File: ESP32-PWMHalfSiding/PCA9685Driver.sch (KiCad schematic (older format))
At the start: 18 parts, among them P601 C A0 A1 A2 A3 A4 A5 A6 A7, P602 C B0 B1 B2 B3 B4 B5 B6 B7, T601 + 12V -, U601 PCA9685, U602 TBD62X83A, U603 TBD62X83A

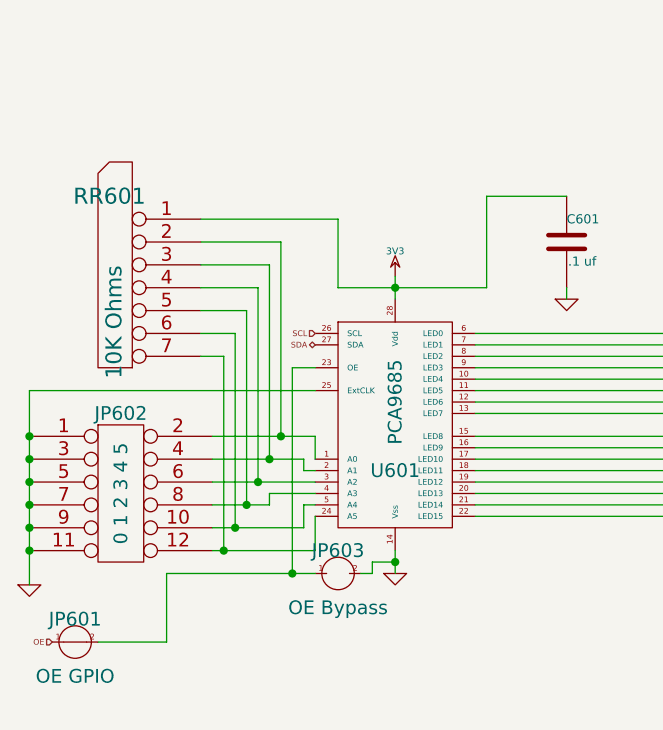
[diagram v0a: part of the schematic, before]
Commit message: Remove unneeded address jumpers from ESP32-PWMHalfSiding and fixup board part labels.
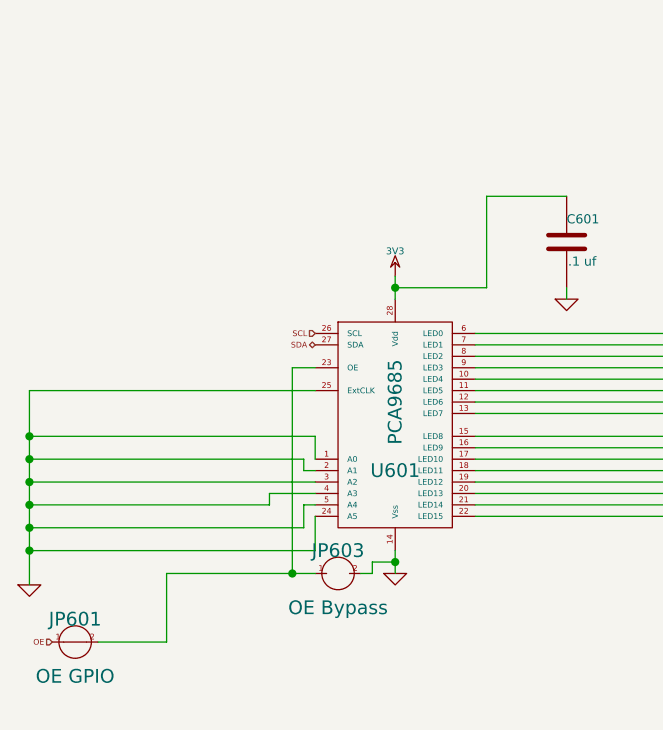
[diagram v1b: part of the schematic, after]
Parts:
- removed JP602: 0 1 2 3 4 5, ~, symbol CONN_6X2
- removed RR601: 10K Ohms, ~, symbol RR6
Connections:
- net GND: now also U601.1 (A0), U601.2 (A1), U601.24 (A5), U601.3 (A2), U601.4 (A3), U601.5 (A4)
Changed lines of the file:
@@
 Sheet 6 6
 Title ""
-Date "1 feb 2020"
+Date "9 feb 2020"
 Rev ""
 Comp ""
@@
 $EndComp
 $Comp
-L CONN_6X2 JP602
-U 1 1 5E35CA23
-P 1600 2700
-F 0 "JP602" H 1600 3050 60  0000 C CNN
-F 1 "0  1  2  3  4  5" V 1600 2700 60  0000 C CNN
-F 2 "~" H 1600 2700 60  0000 C CNN
-F 3 "~" H 1600 2700 60  0000 C CNN
-	1    1600 2700
-	1    0    0    -1
-$EndComp
-$Comp
 L GND #PWR033
 U 1 1 5E35CA24
@@
 $EndComp
 $Comp
-L RR6 RR601
-U 1 1 5E35CA25
-P 1600 1950
-F 0 "RR601" H 1650 2500 70  0000 C CNN
-F 1 "10K Ohms" V 1630 1950 70  0000 C CNN
-F 2 "~" H 1600 1950 60  0000 C CNN
-F 3 "~" H 1600 1950 60  0000 C CNN
-	1    1600 1950
-	-1   0    0    -1
-$EndComp
-$Comp
 L CLOSED JP601
 U 1 1 5E35CA26
@@
 	3200 1800 3200 1400
 Wire Wire Line
-	2550 1800 3200 1800
+	2800 1800 3200 1800
 Connection ~ 2800 1800
 Wire Wire Line
@@
 	5050 4900 5000 4900
 Wire Wire Line
-	1950 1500 2550 1500
-Wire Wire Line
-	2550 1500 2550 1800
-Wire Wire Line
-	2000 2450 2450 2450
+	1200 2450 2450 2450
 Wire Wire Line
 	2450 2450 2450 2550
 Wire Wire Line
-	2000 2950 2450 2950
+	1200 2950 2450 2950
 Wire Wire Line
 	2450 2950 2450 2800
@@
 	2450 2600 2400 2600
 Wire Wire Line
-	2400 2600 2400 2550
-Wire Wire Line
-	2400 2550 2000 2550
+	2400 2550 2400 2600
+Wire Wire Line
+	1200 2550 2400 2550
 Wire Wire Line
 	2450 2750 2400 2750
 Wire Wire Line
-	2400 2850 2000 2850
+	1200 2850 2400 2850
 Wire Wire Line
 	2250 2700 2450 2700
 Wire Wire Line
-	2000 2650 2450 2650
-Wire Wire Line
-	1950 2100 2050 2100
-Wire Wire Line
-	2050 2100 2050 2950
-Connection ~ 2050 2950
-Wire Wire Line
-	1950 2000 2100 2000
-Wire Wire Line
-	2100 2000 2100 2850
-Connection ~ 2100 2850
-Wire Wire Line
-	2150 2750 2150 1900
-Wire Wire Line
-	2150 1900 1950 1900
-Connection ~ 2150 2750
-Wire Wire Line
-	1950 1800 2200 1800
-Connection ~ 2200 2650
-Wire Wire Line
-	2250 2550 2250 1700
-Wire Wire Line
-	2250 1700 1950 1700
-Connection ~ 2250 2550
-Wire Wire Line
-	1950 1600 2300 1600
-Wire Wire Line
-	2300 1600 2300 2450
-Connection ~ 2300 2450
+	1200 2650 2450 2650
 Wire Wire Line
 	1200 2250 1200 3100
@@
 Connection ~ 2800 3000
 Wire Wire Line
-	2400 2750 2400 2850
-Wire Wire Line
-	2200 1800 2200 2650
-Wire Wire Line
-	2250 2700 2250 2750
-Wire Wire Line
-	2250 2750 2000 2750
+	2400 2850 2400 2750
+Wire Wire Line
+	2250 2750 2250 2700
+Wire Wire Line
+	1200 2750 2250 2750
 Connection ~ 2350 3050
 Wire Wire Line

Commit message: BOM for ESP32-PWMHalfSiding
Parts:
- C601: Mouser Part Number (none) -> 21RZ310-RC
- D601: Mouser Part Number (none) -> 625-SB240-E3
- P601, P602: Mouser Part Number (none) -> 651-1725724
- RP601, RP602: Mouser Part Number (none) -> 652-4116R-1LF-1.5K
- T601: Mouser Part Number (none) -> 651-1725656
- U601: Mouser Part Number (none) -> 771-PCA9685PW,118
- U602, U603: Mouser Part Number (none) -> 757-TBD62083APG or 757-TBD62783APG
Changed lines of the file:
@@
 Sheet 6 6
 Title ""
-Date "9 feb 2020"
+Date "11 feb 2020"
 Rev ""
 Comp ""
@@
 F 2 "~" H 2800 2400 60  0000 C CNN
 F 3 "~" H 2800 2400 60  0000 C CNN
+F 4 " 771-PCA9685PW,118" H 2800 2400 60  0001 C CNN "Mouser Part Number"
 	1    2800 2400
 	1    0    0    -1
@@
 F 2 "~" H 3588 1450 30  0000 C CNN
 F 3 "~" H 3550 1600 60  0000 C CNN
+F 4 "21RZ310-RC" H 3550 1600 60  0001 C CNN "Mouser Part Number"
 	1    3550 1600
 	1    0    0    -1
@@
 F 2 "~" H 4800 1100 60  0000 C CNN
 F 3 "~" H 4800 1100 60  0000 C CNN
+F 4 " 757-TBD62083APG or 757-TBD62783APG" H 4800 1100 60  0001 C CNN "Mouser Part Number"
 	1    4800 1100
 	1    0    0    -1
@@
 F 2 "~" H 7300 1050 60  0000 C CNN
 F 3 "~" H 7300 1050 60  0000 C CNN
+F 4 "757-TBD62083APG or 757-TBD62783APG" H 7300 1050 60  0001 C CNN "Mouser Part Number"
 	1    7300 1050
 	1    0    0    -1
@@
 F 2 "~" H 9500 1400 60  0000 C CNN
 F 3 "~" H 9500 1400 60  0000 C CNN
+F 4 "652-4116R-1LF-1.5K" H 9500 1400 60  0001 C CNN "Mouser Part Number"
 	1    9500 1400
 	1    0    0    -1
@@
 F 2 "~" H 9550 3850 60  0000 C CNN
 F 3 "~" H 9550 3850 60  0000 C CNN
+F 4 "652-4116R-1LF-1.5K" H 9550 3850 60  0001 C CNN "Mouser Part Number"
 	1    9550 3850
 	1    0    0    -1
@@
 F 2 "~" H 10600 1450 60  0000 C CNN
 F 3 "~" H 10600 1450 60  0000 C CNN
+F 4 "651-1725724" H 10600 1450 60  0001 C CNN "Mouser Part Number"
 	1    10600 1450
 	1    0    0    -1
@@
 F 2 "~" H 10600 3900 60  0000 C CNN
 F 3 "~" H 10600 3900 60  0000 C CNN
+F 4 "651-1725724" H 10600 3900 60  0001 C CNN "Mouser Part Number"
 	1    10600 3900
 	1    0    0    -1
@@
 F 2 "~" H 3500 5050 60  0000 C CNN
 F 3 "~" H 3500 5050 60  0000 C CNN
+F 4 "625-SB240-E3" H 3500 5050 60  0001 C CNN "Mouser Part Number"
 	1    3500 5050
 	-1   0    0    1
@@
 F 2 "~" H 2500 5150 60  0000 C CNN
 F 3 "~" H 2500 5150 60  0000 C CNN
+F 4 "651-1725656" H 2500 5150 60  0001 C CNN "Mouser Part Number"
 	1    2500 5150
 	-1   0    0    -1

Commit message: ESP32-HalfSiding updates
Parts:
- C601: footprint ~ -> Capacitors_THT:C_Rect_L4.0mm_W2.5mm_P2.50mm; symbol C -> C-RESCUE-ESP32-PWMHalfSiding
- D601: footprint ~ -> Diodes_THT:D_DO-41_SOD81_P7.62mm_Horizontal
- JP601, JP603, JP604, JP605, JP606, JP607, P601, P602, RP601, RP602, T601, U601, U602, U603: footprint ~ -> (none)
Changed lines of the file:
@@
 EESchema Schematic File Version 2
+LIBS:ESP32-PWMHalfSiding-rescue
 LIBS:power
 LIBS:device
@@
 LIBS:memory
 LIBS:xilinx
-LIBS:special
 LIBS:microcontrollers
 LIBS:dsp
@@
 LIBS:pca9685
 LIBS:ESP32-PWMHalfSiding-cache
-EELAYER 27 0
+EELAYER 25 0
 EELAYER END
 $Descr A4 11693 8268
@@
 F 0 "U601" H 2800 2200 60  0000 C CNN
 F 1 "PCA9685" V 2800 2500 60  0000 C CNN
-F 2 "~" H 2800 2400 60  0000 C CNN
+F 2 "" H 2800 2400 60  0001 C CNN
 F 3 "~" H 2800 2400 60  0000 C CNN
 F 4 " 771-PCA9685PW,118" H 2800 2400 60  0001 C CNN "Mouser Part Number"
@@
 $EndComp
 $Comp
-L GND #PWR023
+L GND-RESCUE-ESP32-PWMHalfSiding #PWR023
 U 1 1 5E35CA00
 P 2800 3050
@@
 $EndComp
 $Comp
-L C C601
+L C-RESCUE-ESP32-PWMHalfSiding C601
 U 1 1 5E35CA01
 P 3550 1600
 F 0 "C601" H 3550 1700 40  0000 L CNN
 F 1 ".1 uf" H 3556 1515 40  0000 L CNN
-F 2 "~" H 3588 1450 30  0000 C CNN
+F 2 "Capacitors_THT:C_Rect_L4.0mm_W2.5mm_P2.50mm" H 3588 1450 30  0000 C CNN
 F 3 "~" H 3550 1600 60  0000 C CNN
 F 4 "21RZ310-RC" H 3550 1600 60  0001 C CNN "Mouser Part Number"
@@
 $EndComp
 $Comp
-L GND #PWR024
+L GND-RESCUE-ESP32-PWMHalfSiding #PWR024
 U 1 1 5E35CA02
 P 3550 1850
@@
 F 0 "U602" H 4900 950 60  0000 C CNN
 F 1 "TBD62X83A" H 5050 1200 60  0000 C CNN
-F 2 "~" H 4800 1100 60  0000 C CNN
+F 2 "" H 4800 1100 60  0001 C CNN
 F 3 "~" H 4800 1100 60  0000 C CNN
 F 4 " 757-TBD62083APG or 757-TBD62783APG" H 4800 1100 60  0001 C CNN "Mouser Part Number"
@@
 F 0 "U602" H 4900 1450 60  0000 C CNN
 F 1 "TBD62X83A" H 5050 1700 60  0000 C CNN
-F 2 "~" H 4800 1600 60  0000 C CNN
+F 2 "" H 4800 1600 60  0001 C CNN
 F 3 "~" H 4800 1600 60  0000 C CNN
 	2    4800 1600
@@
 F 0 "U602" H 4900 1950 60  0000 C CNN
 F 1 "TBD62X83A" H 5050 2200 60  0000 C CNN
-F 2 "~" H 4800 2100 60  0000 C CNN
+F 2 "" H 4800 2100 60  0001 C CNN
 F 3 "~" H 4800 2100 60  0000 C CNN
 	3    4800 2100
@@
 F 0 "U602" H 4900 2450 60  0000 C CNN
 F 1 "TBD62X83A" H 5050 2700 60  0000 C CNN
-F 2 "~" H 4800 2600 60  0000 C CNN
+F 2 "" H 4800 2600 60  0001 C CNN
 F 3 "~" H 4800 2600 60  0000 C CNN
 	4    4800 2600
@@
 F 0 "U602" H 4900 2950 60  0000 C CNN
 F 1 "TBD62X83A" H 5050 3200 60  0000 C CNN
-F 2 "~" H 4800 3100 60  0000 C CNN
+F 2 "" H 4800 3100 60  0001 C CNN
 F 3 "~" H 4800 3100 60  0000 C CNN
 	5    4800 3100
@@
 F 0 "U602" H 4900 3450 60  0000 C CNN
 F 1 "TBD62X83A" H 5050 3700 60  0000 C CNN
-F 2 "~" H 4800 3600 60  0000 C CNN
+F 2 "" H 4800 3600 60  0001 C CNN
 F 3 "~" H 4800 3600 60  0000 C CNN
 	6    4800 3600
@@
 F 0 "U602" H 4900 3950 60  0000 C CNN
 F 1 "TBD62X83A" H 5050 4200 60  0000 C CNN
-F 2 "~" H 4800 4100 60  0000 C CNN
+F 2 "" H 4800 4100 60  0001 C CNN
 F 3 "~" H 4800 4100 60  0000 C CNN
 	7    4800 4100
@@
 F 0 "U602" H 4900 4450 60  0000 C CNN
 F 1 "TBD62X83A" H 5050 4700 60  0000 C CNN
-F 2 "~" H 4800 4600 60  0000 C CNN
+F 2 "" H 4800 4600 60  0001 C CNN
 F 3 "~" H 4800 4600 60  0000 C CNN
 	8    4800 4600
@@
 F 0 "U603" H 7400 900 60  0000 C CNN
 F 1 "TBD62X83A" H 7550 1150 60  0000 C CNN
-F 2 "~" H 7300 1050 60  0000 C CNN
+F 2 "" H 7300 1050 60  0001 C CNN
 F 3 "~" H 7300 1050 60  0000 C CNN
 F 4 "757-TBD62083APG or 757-TBD62783APG" H 7300 1050 60  0001 C CNN "Mouser Part Number"
@@
 F 0 "U603" H 7400 1400 60  0000 C CNN
 F 1 "TBD62X83A" H 7550 1650 60  0000 C CNN
-F 2 "~" H 7300 1550 60  0000 C CNN
+F 2 "" H 7300 1550 60  0001 C CNN
 F 3 "~" H 7300 1550 60  0000 C CNN
 	2    7300 1550
@@
 F 0 "U603" H 7400 1900 60  0000 C CNN
 F 1 "TBD62X83A" H 7550 2150 60  0000 C CNN
-F 2 "~" H 7300 2050 60  0000 C CNN
+F 2 "" H 7300 2050 60  0001 C CNN
 F 3 "~" H 7300 2050 60  0000 C CNN
 	3    7300 2050
@@
 F 0 "U603" H 7400 2400 60  0000 C CNN
 F 1 "TBD62X83A" H 7550 2650 60  0000 C CNN
-F 2 "~" H 7300 2550 60  0000 C CNN
+F 2 "" H 7300 2550 60  0001 C CNN
 F 3 "~" H 7300 2550 60  0000 C CNN
 	4    7300 2550
@@
 F 0 "U603" H 7400 2900 60  0000 C CNN
 F 1 "TBD62X83A" H 7550 3150 60  0000 C CNN
-F 2 "~" H 7300 3050 60  0000 C CNN
+F 2 "" H 7300 3050 60  0001 C CNN
 F 3 "~" H 7300 3050 60  0000 C CNN
 	5    7300 3050
@@
 F 0 "U603" H 7400 3400 60  0000 C CNN
 F 1 "TBD62X83A" H 7550 3650 60  0000 C CNN
-F 2 "~" H 7300 3550 60  0000 C CNN
+F 2 "" H 7300 3550 60  0001 C CNN
 F 3 "~" H 7300 3550 60  0000 C CNN
 	6    7300 3550
@@
 F 0 "U603" H 7400 3900 60  0000 C CNN
 F 1 "TBD62X83A" H 7550 4150 60  0000 C CNN
-F 2 "~" H 7300 4050 60  0000 C CNN
+F 2 "" H 7300 4050 60  0001 C CNN
 F 3 "~" H 7300 4050 60  0000 C CNN
 	7    7300 4050
@@
 F 0 "U603" H 7400 4400 60  0000 C CNN
 F 1 "TBD62X83A" H 7550 4650 60  0000 C CNN
-F 2 "~" H 7300 4550 60  0000 C CNN
+F 2 "" H 7300 4550 60  0001 C CNN
 F 3 "~" H 7300 4550 60  0000 C CNN
 	8    7300 4550
@@
 F 0 "RP601" H 9500 1850 40  0000 C CNN
 F 1 "1.5K Ohms" H 9500 950 40  0000 C CNN
-F 2 "~" H 9500 1400 60  0000 C CNN
+F 2 "" H 9500 1400 60  0001 C CNN
 F 3 "~" H 9500 1400 60  0000 C CNN
 F 4 "652-4116R-1LF-1.5K" H 9500 1400 60  0001 C CNN "Mouser Part Number"
@@
 F 0 "RP602" H 9550 4300 40  0000 C CNN
 F 1 "1.5K Ohms" H 9550 3400 40  0000 C CNN
-F 2 "~" H 9550 3850 60  0000 C CNN
+F 2 "" H 9550 3850 60  0001 C CNN
 F 3 "~" H 9550 3850 60  0000 C CNN
 F 4 "652-4116R-1LF-1.5K" H 9550 3850 60  0001 C CNN "Mouser Part Number"
@@
 F 0 "JP605" H 4850 5050 40  0000 L CNN
 F 1 "CK A CA" H 4800 5250 40  0000 C CNN
-F 2 "~" H 4800 5150 60  0000 C CNN
+F 2 "" H 4800 5150 60  0001 C CNN
 F 3 "~" H 4800 5150 60  0000 C CNN
 	1    4800 5150
@@
 F 0 "JP607" H 7350 5000 40  0000 L CNN
 F 1 "CK B CA" H 7300 5200 40  0000 C CNN
-F 2 "~" H 7300 5100 60  0000 C CNN
+F 2 "" H 7300 5100 60  0001 C CNN
 F 3 "~" H 7300 5100 60  0000 C CNN
 	1    7300 5100
@@
 F 0 "JP604" H 4850 600 40  0000 L CNN
 F 1 "CK A CA" H 4800 800 40  0000 C CNN
-F 2 "~" H 4800 700 60  0000 C CNN
+F 2 "" H 4800 700 60  0001 C CNN
 F 3 "~" H 4800 700 60  0000 C CNN
 	1    4800 700
@@
 F 0 "JP606" H 7350 600 40  0000 L CNN
 F 1 "CK B CA" H 7300 800 40  0000 C CNN
-F 2 "~" H 7300 700 60  0000 C CNN
+F 2 "" H 7300 700 60  0001 C CNN
 F 3 "~" H 7300 700 60  0000 C CNN
 	1    7300 700
@@
 F 0 "P601" V 10550 1450 60  0000 C CNN
 F 1 "C A0 A1 A2 A3 A4 A5 A6 A7" V 10650 1450 60  0000 C CNN
-F 2 "~" H 10600 1450 60  0000 C CNN
+F 2 "" H 10600 1450 60  0001 C CNN
 F 3 "~" H 10600 1450 60  0000 C CNN
 F 4 "651-1725724" H 10600 1450 60  0001 C CNN "Mouser Part Number"
@@
 F 0 "P602" V 10550 3900 60  0000 C CNN
 F 1 "C B0 B1 B2 B3 B4 B5 B6 B7" V 10650 3900 60  0000 C CNN
-F 2 "~" H 10600 3900 60  0000 C CNN
+F 2 "" H 10600 3900 60  0001 C CNN
 F 3 "~" H 10600 3900 60  0000 C CNN
 F 4 "651-1725724" H 10600 3900 60  0001 C CNN "Mouser Part Number"
@@
 $EndComp
 $Comp
-L GND #PWR029
+L GND-RESCUE-ESP32-PWMHalfSiding #PWR029
 U 1 1 5E35CA1F
 P 4550 5350
@@
 $EndComp
 $Comp
-L GND #PWR030
+L GND-RESCUE-ESP32-PWMHalfSiding #PWR030
 U 1 1 5E35CA20
 P 7050 5300
@@
 $EndComp
 $Comp
-L GND #PWR031
+L GND-RESCUE-ESP32-PWMHalfSiding #PWR031
 U 1 1 5E35CA21
 P 7550 750
@@
 $EndComp
 $Comp
-L GND #PWR032
+L GND-RESCUE-ESP32-PWMHalfSiding #PWR032
 U 1 1 5E35CA22
 P 5050 750
@@
 $EndComp
 $Comp
-L GND #PWR033
+L GND-RESCUE-ESP32-PWMHalfSiding #PWR033
 U 1 1 5E35CA24
 P 1200 3100
@@
 F 0 "JP601" H 1400 3250 60  0000 C CNN
 F 1 "OE GPIO" H 1400 3000 60  0000 C CNN
-F 2 "~" H 1400 3250 60  0000 C CNN
+F 2 "" H 1400 3250 60  0001 C CNN
 F 3 "~" H 1400 3250 60  0000 C CNN
 	1    1400 3250
@@
 F 0 "JP603" H 2550 2950 60  0000 C CNN
 F 1 "OE Bypass" H 2550 2700 60  0000 C CNN
-F 2 "~" H 2550 2950 60  0000 C CNN
+F 2 "" H 2550 2950 60  0001 C CNN
 F 3 "~" H 2550 2950 60  0000 C CNN
 	1    2550 2950
@@
 	2450 2600 2400 2600
 Wire Wire Line
-	2400 2550 2400 2600
-Wire Wire Line
-	1200 2550 2400 2550
+	2400 2600 2400 2550
+Wire Wire Line
+	2400 2550 1200 2550
 Wire Wire Line
 	2450 2750 2400 2750
@@
 F 0 "D601" H 3500 5150 40  0000 C CNN
 F 1 "SB240E" H 3500 4950 40  0000 C CNN
-F 2 "~" H 3500 5050 60  0000 C CNN
+F 2 "Diodes_THT:D_DO-41_SOD81_P7.62mm_Horizontal" H 3500 5050 60  0001 C CNN
 F 3 "~" H 3500 5050 60  0000 C CNN
 F 4 "625-SB240-E3" H 3500 5050 60  0001 C CNN "Mouser Part Number"
@@
 F 0 "T601" V 2450 5150 40  0000 C CNN
 F 1 "+ 12V -" V 2550 5150 40  0000 C CNN
-F 2 "~" H 2500 5150 60  0000 C CNN
+F 2 "" H 2500 5150 60  0001 C CNN
 F 3 "~" H 2500 5150 60  0000 C CNN
 F 4 "651-1725656" H 2500 5150 60  0001 C CNN "Mouser Part Number"
@@
 	2850 5050 3300 5050
 $Comp
-L GND #PWR035
+L GND-RESCUE-ESP32-PWMHalfSiding #PWR035
 U 1 1 5E35CA2B
 P 2850 5350
